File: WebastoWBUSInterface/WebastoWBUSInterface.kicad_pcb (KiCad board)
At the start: 2 copper layers, 50 x 24 mm, 16 parts, among them J1 FTDI Interface, J2 WBUS, Q1 BC548, Q2 BC548, Q3 BC548, Q4 BC557

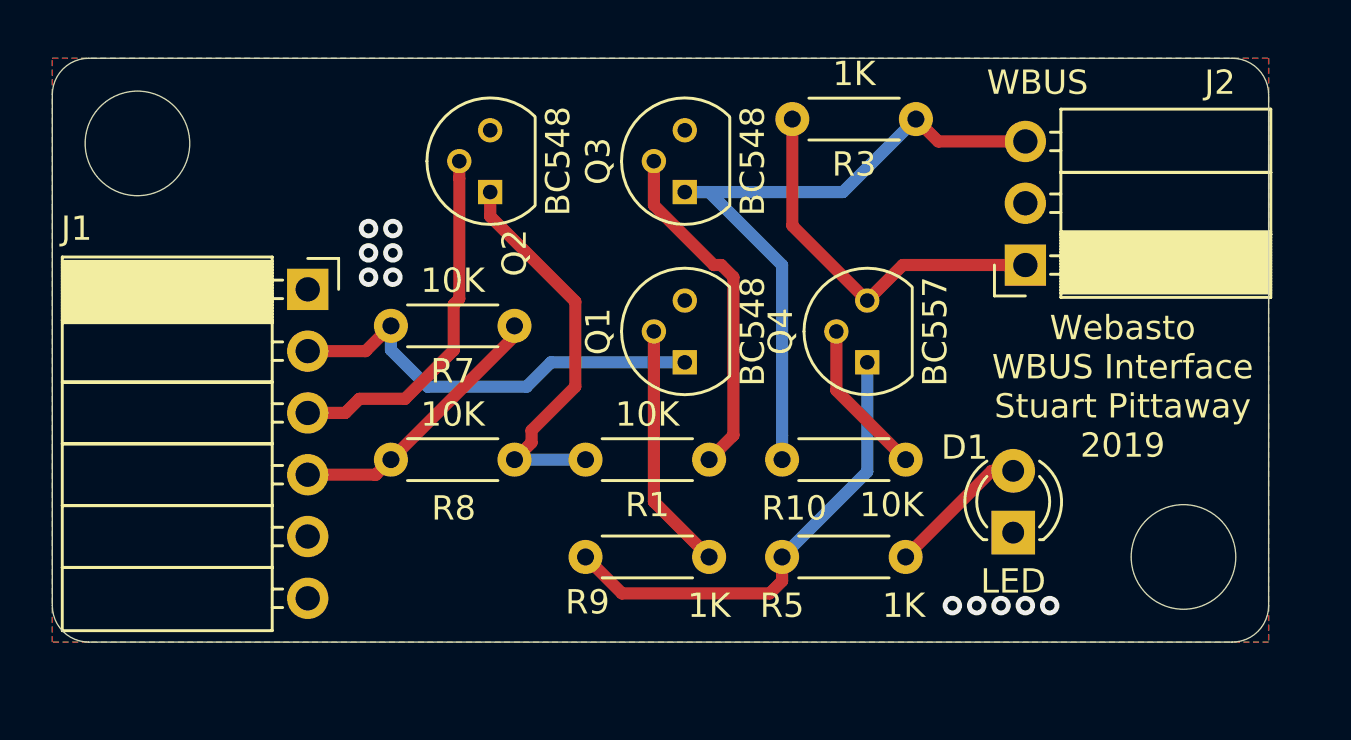
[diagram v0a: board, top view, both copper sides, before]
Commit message: Larger resistor hole sizes
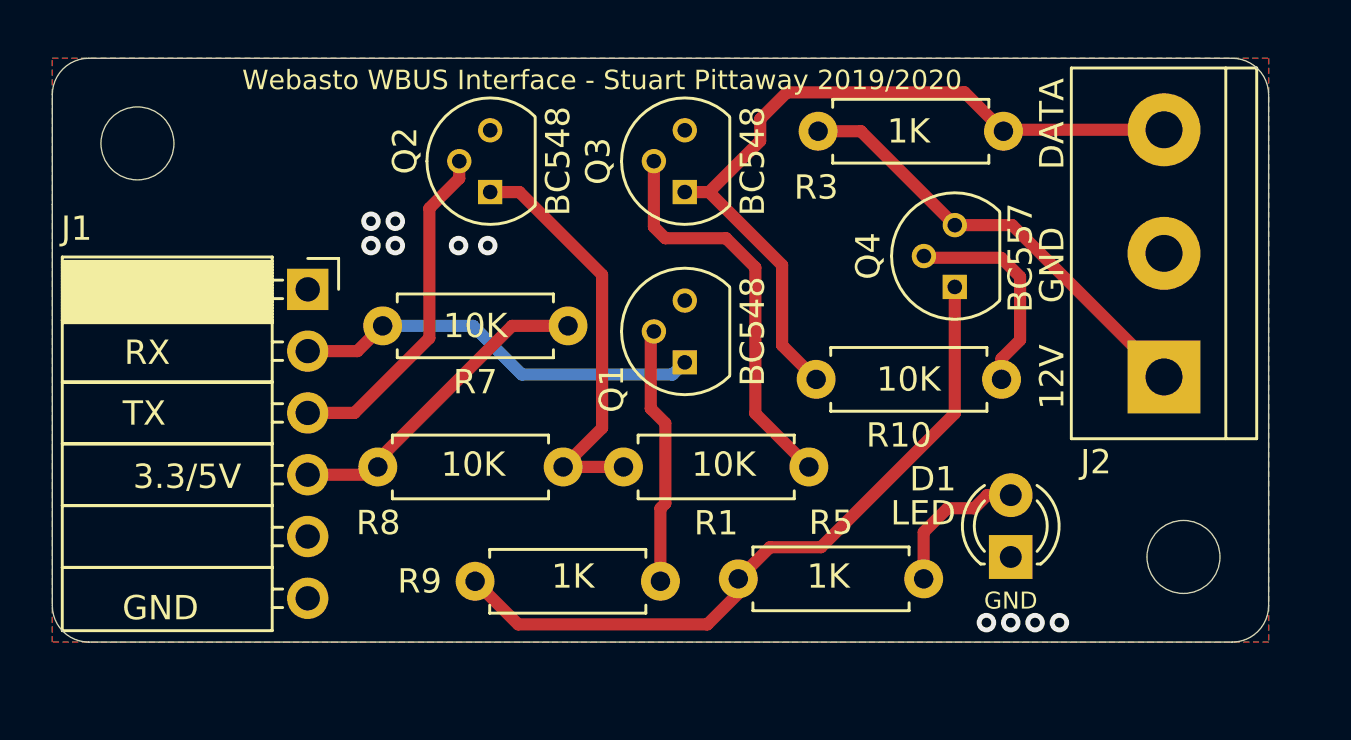
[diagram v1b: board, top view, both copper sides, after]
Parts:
- J1: value FTDI Interface -> Serial Interface
- J2: footprint Socket_Strips:Socket_Strip_Angled_1x03_Pitch2.54mm -> Connectors_Terminal_Blocks:TerminalBlock_bornier-3_P5.08mm
- R1, R10, R3, R5, R7, R8, R9: footprint Resistors_THT:R_Axial_DIN0204_L3.6mm_D1.6mm_P5.08mm_Horizontal -> Resistors_THT:R_Axial_DIN0207_L6.3mm_D2.5mm_P7.62mm_Horizontal
- REF** (x2): value MountingHole_4.3mm_M4 -> MountingHole_3mm; footprint Mounting_Holes:MountingHole_4.3mm_M4 -> Mounting_Holes:MountingHole_3mm
- moved J2 7.32 mm to (110.7, 89.1), turned to 90 degrees
- moved Q4 4.75 mm to (102.1, 85.4)
- moved R1 4.11 mm to (96.1, 92.8)
- moved R3 3.63 mm to (104.1, 79.0)
- moved R10 3.58 mm to (96.4, 89.2)
- moved R9 2.24 mm to (90.0, 97.5)
- moved R7 2.20 mm to (86.2, 87.0)
- moved R8 2.02 mm to (86.0, 92.8)
- moved R5 2.01 mm to (93.2, 97.4)
- moved D1 1.00 mm to (104.4, 96.5)
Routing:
- net Net-(Q4-Pad1): track 19.4 -> 29.6 mm
- net WBUS: track 28.9 -> 32.1 mm
- net +12V: track 15.8 -> 18.4 mm
- net Net-(Q3-Pad2): track 14.2 -> 16.7 mm
- net Net-(Q4-Pad2): track 6.45 -> 8.84 mm
- net +5V: track 11.3 -> 13.4 mm
- net Net-(Q2-Pad1): track 16.4 -> 17.5 mm
- net RX: track 18.0 -> 17.0 mm
- net TX: track 14.9 -> 14.1 mm
- net GND: vias 11 -> 10
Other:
- net class Default: clearance 0.2 -> 0.3
- rule trace_clearance: 0.2 -> 0.3
- rule trace_min: 0.2 -> 0.3
- board text added: "3.3/5V"
- board text added: "DATA"
- board text added: "WBUS Interface"
- board text added: "Webasto WBUS Interface - Stuart Pittaway 2019/2020"
- board text removed: "5V"
- board text removed: "WBUS DATA"
- board text removed: "Webasto WBUS Interface Stuart Pittaway 2019"

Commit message: JLCPCB SMD board for full assembly
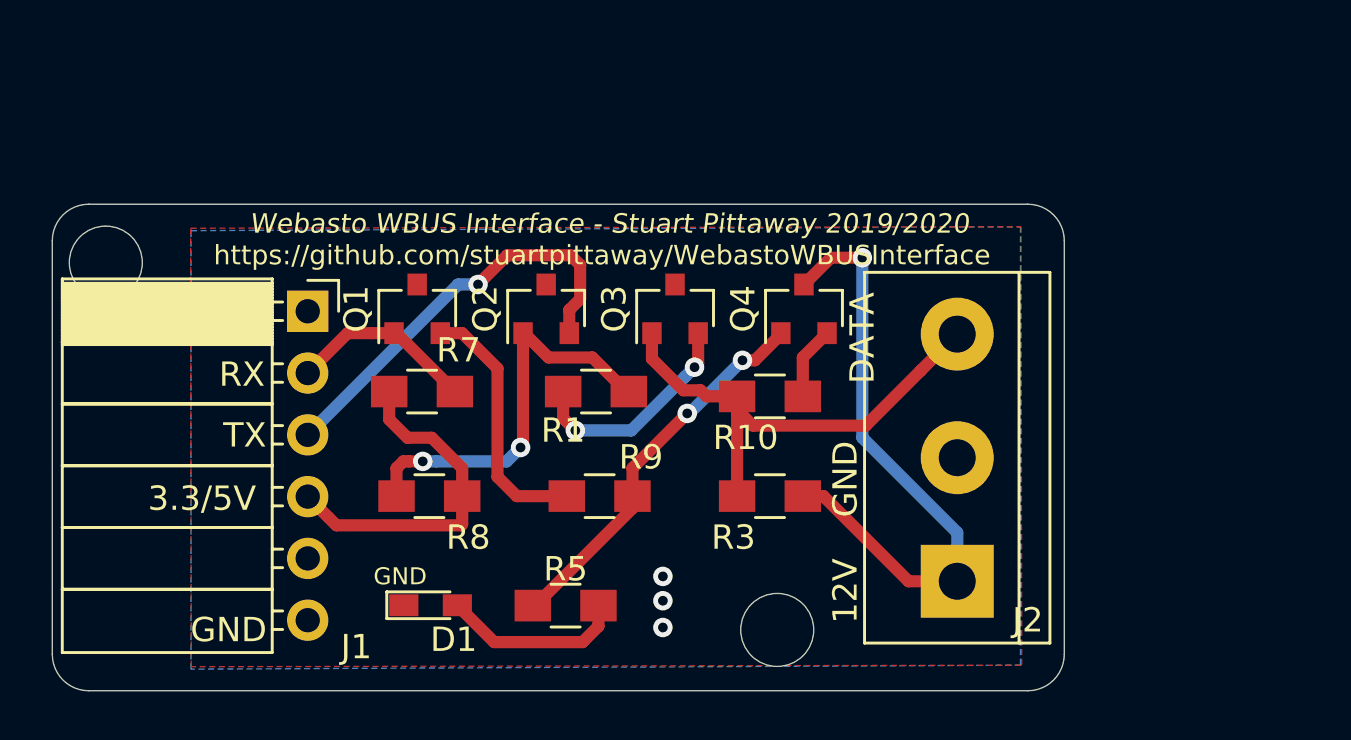
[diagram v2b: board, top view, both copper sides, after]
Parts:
- removed the REF** at (68.5, 79.5)
- removed the REF** at (111.5, 96.5)
- added REF**: MountingHole_3mm, Mounting_Holes:MountingHole_3mm, F.Cu at (67.2, 84.4)
- added REF**: MountingHole_3mm, Mounting_Holes:MountingHole_3mm, F.Cu at (94.8, 99.5)
- D1: footprint LEDs:LED_D3.0mm -> LEDs:LED_0603_HandSoldering
- J1: value Serial Interface -> FTDI Interface
- Q1, Q2, Q3: value BC548 -> S9013; footprint TO_SOT_Packages_THT:TO-92_Molded_Narrow -> TO_SOT_Packages_SMD:SOT-23
- Q4: value BC557 -> S9015; footprint TO_SOT_Packages_THT:TO-92_Molded_Narrow -> TO_SOT_Packages_SMD:SOT-23
- R1, R10, R3, R5, R7, R8, R9: footprint Resistors_THT:R_Axial_DIN0207_L6.3mm_D2.5mm_P7.62mm_Horizontal -> Resistors_SMD:R_0805_HandSoldering
- moved D1 23.9 mm to (80.5, 98.5), turned to 0 degrees
- moved R3 17.8 mm to (94.5, 94.0), turned to 0 degrees
- moved J2 12.0 mm to (102.2, 97.5)
- moved Q1 11.2 mm to (80.0, 86.3)
- moved R1 9.28 mm to (87.3, 89.7), turned to 0 degrees
- moved R5 7.18 mm to (86.1, 98.5)
- moved R7 6.58 mm to (80.2, 89.7), turned to 0 degrees
- moved Q4 6.26 mm to (95.9, 86.3)
- moved R8 5.63 mm to (80.5, 94.0), turned to 0 degrees
- moved Q2 5.32 mm to (85.3, 86.3)
- moved Q3 4.82 mm to (90.6, 86.3)
- moved R9 4.30 mm to (87.5, 94.0), turned to 0 degrees
- moved R10 2.02 mm to (94.5, 89.9)
- moved J1 0.90 mm to (75.5, 86.4)
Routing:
- net Net-(Q4-Pad1): track 29.6 -> 15.8 mm, vias 0 -> 2
- net WBUS: track 32.1 -> 20.7 mm
- net RX: track 17.0 -> 7.72 mm
- net Net-(Q3-Pad2): track 16.7 -> 9.25 mm, vias 0 -> 2
- net +12V: track 18.4 -> 25.6 mm, vias 0 -> 1
- net Net-(Q4-Pad2): track 8.84 -> 3.01 mm
- net TX: track 14.1 -> 17.4 mm, vias 0 -> 1
- net Net-(D1-Pad2): track 6.13 -> 7.55 mm
- net Net-(Q2-Pad1): track 17.5 -> 16.7 mm, vias 0 -> 2
- net +5V: track 13.4 -> 14.1 mm
- net GND: vias 10 -> 3
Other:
- board size 50 x 24 mm -> 41.6 x 20 mm
